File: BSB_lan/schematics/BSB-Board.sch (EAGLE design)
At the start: 18 parts, among them Q1 BC107, X1 SSW-106-02-S-S, X2 SSW-116-02-S-S, X3 SSW-108-02-S-S

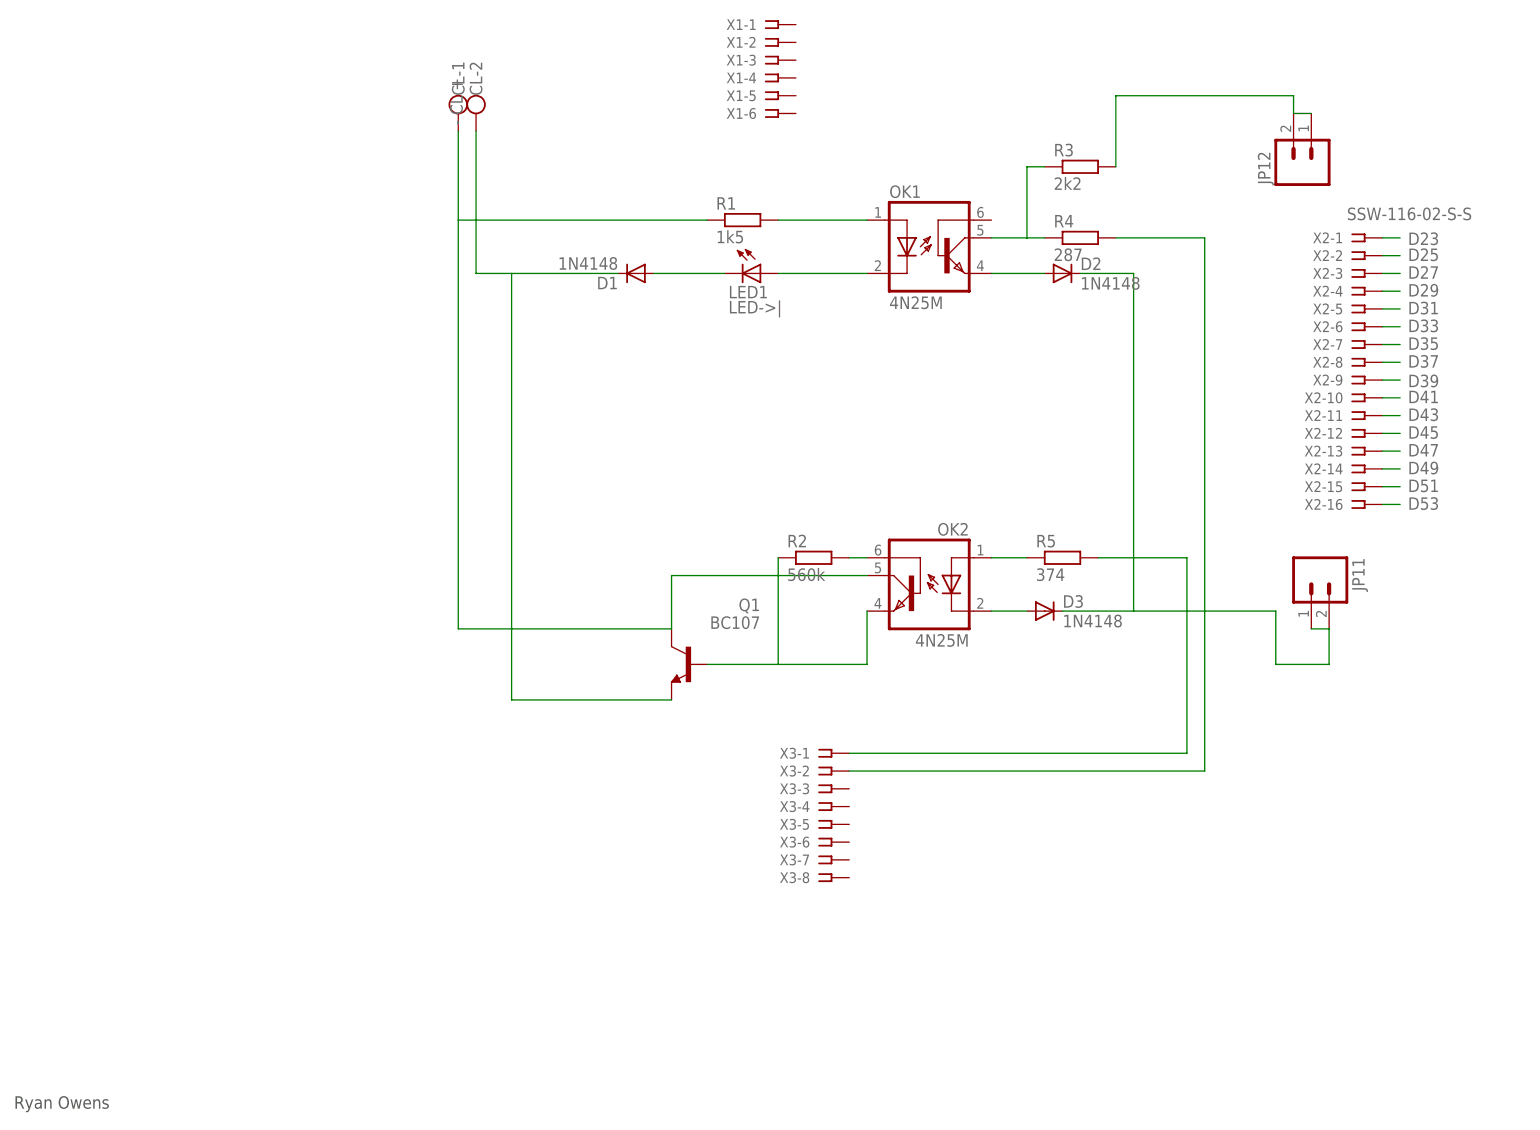
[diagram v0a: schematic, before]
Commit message: Add files via upload
Schematic:
- fix ERC warnings in schematic (missing junctions - use NET instead of WIRE).
Board:
- rearrange components
- use thicker wires
- route single-sided

TODO:
- use smaller packages for diodes (they are 1N4148!)
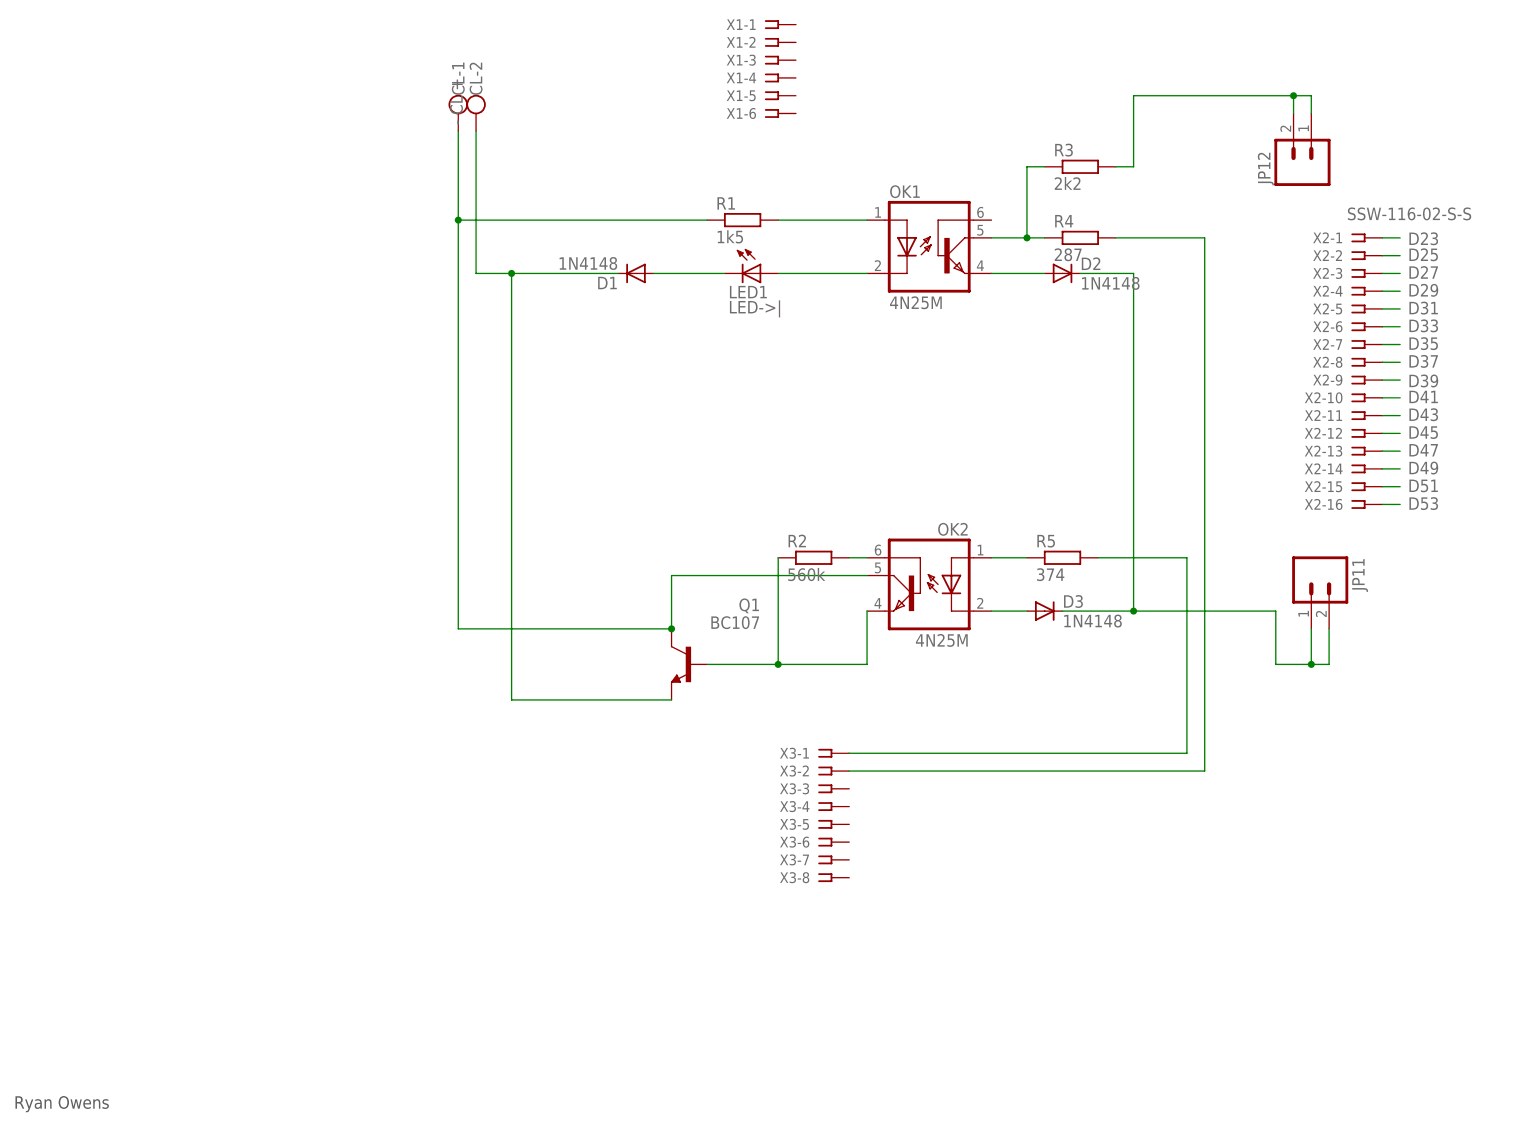
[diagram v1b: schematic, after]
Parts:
- R1, R3, R4, R5: device eagle-ltspice:R0207/10 -> eagle-ltspice:R0204/7
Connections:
- net N$10 renamed GND
